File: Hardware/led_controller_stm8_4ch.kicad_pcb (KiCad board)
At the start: 2 copper layers, 79.5 x 23 mm, 27 parts, among them J1 LEDS, J2 STM8_Prog_Conn, J3 EXT_BTN, Q1 2N7002, Q2 2N7002, Q3 2N7002, Q4 2N7002, SW1 SW_Push, U1 STM8S103F3

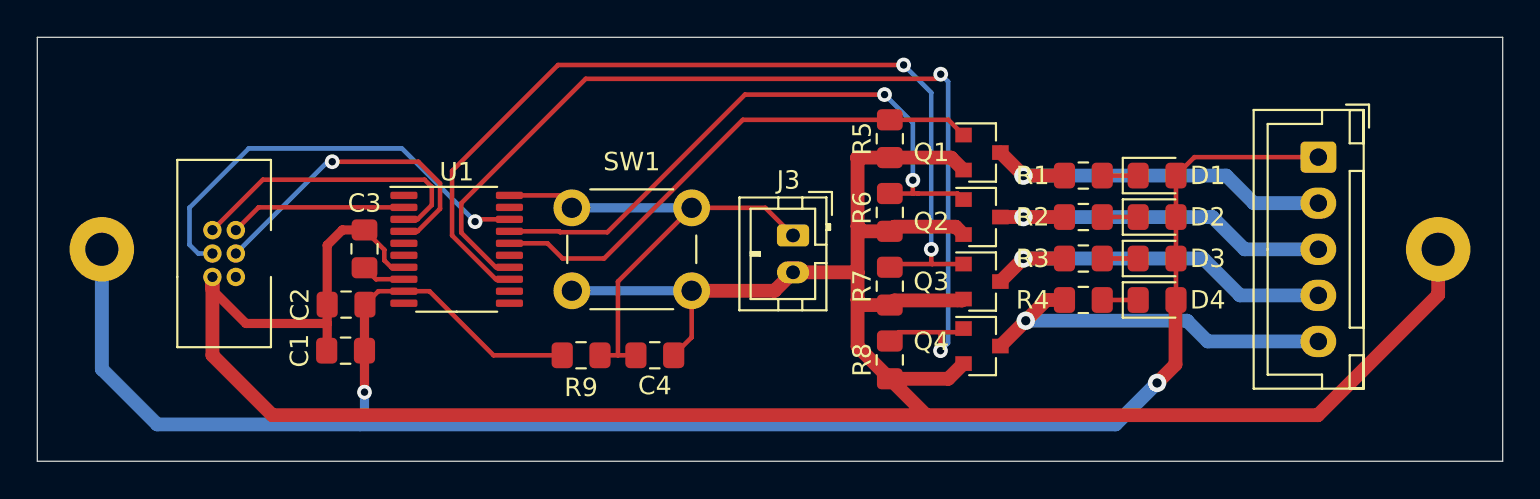
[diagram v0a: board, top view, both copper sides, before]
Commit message: add battery protection
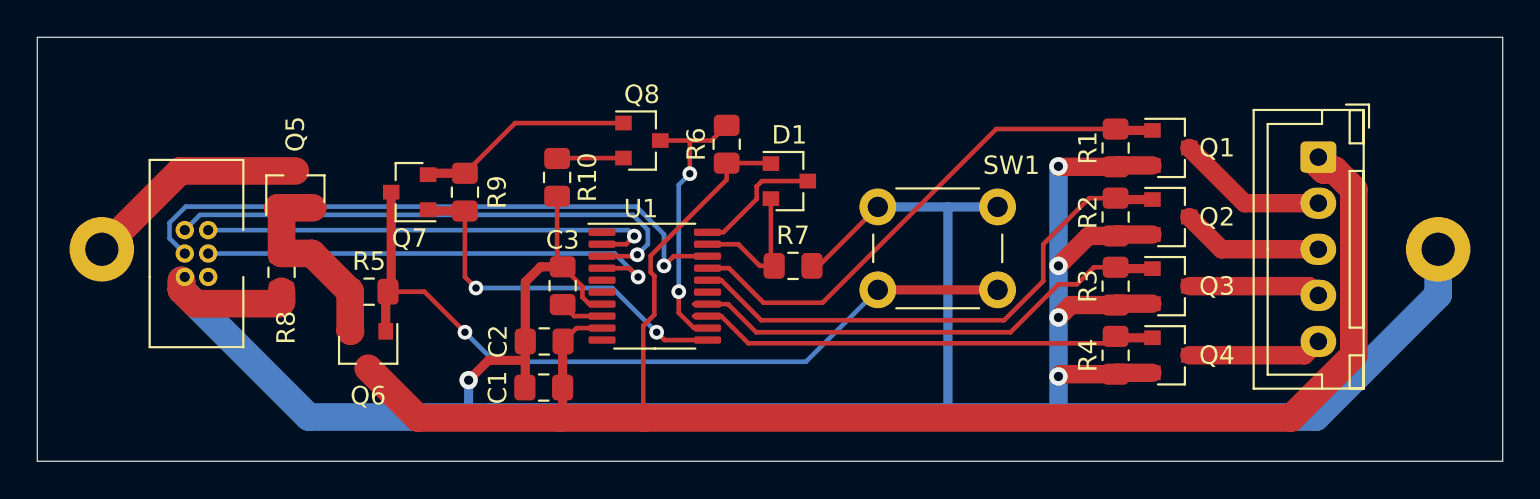
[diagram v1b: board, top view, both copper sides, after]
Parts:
- removed C4: 0.1uF, Capacitor_SMD:C_0805_2012Metric_Pad1.15x1.40mm_HandSolder
- removed D2, D3, D4: LED, LED_SMD:LED_0805_2012Metric_Pad1.15x1.40mm_HandSolder
- removed the J2 at (108.5, 62.0)
- removed J3: EXT_BTN, Connector_JST:JST_PH_B2B-PH-K_1x02_P2.00mm_Vertical
- removed the R1 at (155.8, 56.5)
- added J1: STM8_Prog_Conn, local:IDC-1.27-6P, F.Cu at (107.0, 62.0)
- added Q5: IRLML6401, Package_TO_SOT_SMD:SOT-23, F.Cu at (113.0, 57.2)
- added Q6: IRLML6401, Package_TO_SOT_SMD:SOT-23, F.Cu at (117.0, 66.0)
- added Q7: 2N7002, Package_TO_SOT_SMD:SOT-23, F.Cu at (119.2, 57.4)
- added Q8: MMBT3904, Package_TO_SOT_SMD:SOT-23, F.Cu at (131.8, 54.6)
- added R10: 100, Resistor_SMD:R_0805_2012Metric_Pad1.15x1.40mm_HandSolder, F.Cu at (127.2, 56.6)
- added R5: 150k, Resistor_SMD:R_0805_2012Metric_Pad1.15x1.40mm_HandSolder, F.Cu at (117.0, 62.8)
- D1: value LED -> BAV99; footprint LED_SMD:LED_0805_2012Metric_Pad1.15x1.40mm_HandSolder -> Package_TO_SOT_SMD:SOT-23
- Q1, Q2, Q3, Q4: value 2N7002 -> AO3400A
- R1: renamed from R5; value R -> 10k
- R2, R3, R4: value R -> 10k
- R6: value R -> 15k
- R7, R8: value R -> 150k
- R9: value 12k -> 150k
- moved R8 33.3 mm to (112.2, 61.8)
- moved D1 20.0 mm to (139.8, 56.8)
- moved SW1 16.6 mm to (144.6, 58.2)
- moved R1 12.3 mm to (157.5, 55.0)
- moved C1 10.9 mm to (126.5, 68.0)
- moved C2 10.9 mm to (126.5, 65.5)
- moved C3 10.9 mm to (127.5, 62.5)
- moved U1 10.9 mm to (132.5, 62.5)
- moved R9 10.9 mm to (122.2, 57.4), turned to 90 degrees
- moved Q4 10.3 mm to (160.5, 66.2)
- moved Q1 10.3 mm to (160.5, 55.0)
- moved Q3 10.3 mm to (160.5, 62.5)
- moved Q2 10.2 mm to (160.5, 58.8)
- moved R6 9.59 mm to (136.4, 54.8), turned to 90 degrees
- moved R7 5.36 mm to (140.0, 61.4), turned to 0 degrees
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- renumbered J1 to J2
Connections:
- BT1 pad 1: +BATT -> Net-(BT1-Pad1)
- D1 pad 1: Net-(D1-Pad1) -> +BATT
- D1 pad 2: +BATT -> /BAT_ADC_2
- J2 pad 3: Net-(J1-Pad3) -> Net-(J2-Pad3)
- J2 pad 4: Net-(J1-Pad4) -> Net-(J2-Pad4)
- J2 pad 5: Net-(J1-Pad5) -> Net-(J2-Pad5)
- Q2 pad 3: Net-(J1-Pad3) -> Net-(J2-Pad3)
- Q3 pad 3: Net-(J1-Pad4) -> Net-(J2-Pad4)
- Q4 pad 3: Net-(J1-Pad5) -> Net-(J2-Pad5)
- R2 pad 1: Net-(D2-Pad1) -> /CH2
- R2 pad 2: Net-(J1-Pad3) -> GND
- R3 pad 1: Net-(D3-Pad1) -> /CH3
- R3 pad 2: Net-(J1-Pad4) -> GND
- R4 pad 1: Net-(D4-Pad1) -> /CH4
- R4 pad 2: Net-(J1-Pad5) -> GND
- R6 pad 1: /CH2 -> +BATT
- R6 pad 2: GND -> /BTN
- R7 pad 1: /CH3 -> /BAT_ADC_2
- R8 pad 1: /CH4 -> Net-(Q5-Pad1)
- R9 pad 1: +BATT -> /PWR_EN
- R9 pad 2: /BTN -> Net-(Q7-Pad2)
- SW1 pad 1: /BTN -> GND
- SW1 pad 2: GND -> Net-(Q6-Pad1)
- U1 pad 11: (no net) -> /PWR_EN
- U1 pad 12: (no net) -> /BTN
- U1 pad 13: /CH3 -> /CH4
- U1 pad 14: /CH4 -> /CH3
- U1 pad 16: /CH1 -> /CH2
- U1 pad 17: /CH2 -> /CH1
- U1 pad 19: (no net) -> /BAT_ADC_2
- U1 pad 20: /BTN -> /BAT_ADC_1
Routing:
- net Net-(Q6-Pad1): track 0.00 -> 43.9 mm, vias 0 -> 1
- net /CH4: track 54.5 -> 25.7 mm, vias 2 -> 0
- net /CH3: track 50.0 -> 27.0 mm, vias 2 -> 0
- net Net-(J1-Pad5): track 20.9 -> 0.00 mm, vias 1 -> 0
- net Net-(J1-Pad4): track 20.8 -> 0.00 mm, vias 1 -> 0
- net Net-(J1-Pad3): track 20.2 -> 0.00 mm, vias 1 -> 0
- net /PWR_EN: track 0.00 -> 20.2 mm, vias 0 -> 2
- net /MCU_TX: track 9.63 -> 25.2 mm, vias 0 -> 1
- net /MCU_RX: track 16.0 -> 29.3 mm, vias 0 -> 1
- net /BTN: track 27.9 -> 15.4 mm, vias 0 -> 2
- net Net-(J2-Pad2): track 20.6 -> 8.24 mm, vias 1 -> 0
- net Net-(BT1-Pad1): track 0.00 -> 12.3 mm
- net +BATT: track 104.8 -> 92.8 mm, vias 2 -> 0
- net Net-(Q7-Pad2): track 0.00 -> 11.8 mm
- net Net-(Q5-Pad1): track 0.00 -> 11.2 mm
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
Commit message: fix PWR_EN pin
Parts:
- moved R10 10.7 mm to (136.6, 51.4), turned to 0 degrees
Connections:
- U1 pad 1: (no net) -> /PWR_EN
- U1 pad 11: /PWR_EN -> (no net)
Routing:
- net /PWR_EN: track 20.2 -> 9.94 mm, vias 2 -> 0
- net GND: track 163.8 -> 170.9 mm
- net Net-(Q8-Pad2): track 3.61 -> 6.72 mm
- net /SWIM: track 34.1 -> 35.7 mm
